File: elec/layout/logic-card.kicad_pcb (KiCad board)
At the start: 2 copper layers, 40 x 40 mm, 0 parts

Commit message: progress
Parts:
- added C1: 1uF, Capacitor_SMD:C_0402_1005Metric, F.Cu at (84.7, 136.4)
- added C10: 1uF, Capacitor_SMD:C_0402_1005Metric, F.Cu at (123.4, 146.3)
- added C11: 100nF, Capacitor_SMD:C_0402_1005Metric, F.Cu at (123.4, 134.4)
- added C12: 100nF, Capacitor_SMD:C_0402_1005Metric, F.Cu at (123.4, 142.4)
- added C13: 100nF, Capacitor_SMD:C_0402_1005Metric, F.Cu at (128.3, 146.3)
- added C14: 1uF, Capacitor_SMD:C_0402_1005Metric, F.Cu at (117.0, 149.6)
- added C2: 1uF, Capacitor_SMD:C_0402_1005Metric, F.Cu at (117.0, 145.6)
- added C3: 20pF, Capacitor_SMD:C_0402_1005Metric, F.Cu at (111.9, 146.7)
- added C4: 20pF, Capacitor_SMD:C_0402_1005Metric, F.Cu at (119.8, 146.7)
- added C5: 100nF, Capacitor_SMD:C_0402_1005Metric, F.Cu at (106.1, 145.0)
- added C6: 100nF, Capacitor_SMD:C_0402_1005Metric, F.Cu at (123.4, 138.4)
- added C7: 100nF, Capacitor_SMD:C_0402_1005Metric, F.Cu at (128.3, 142.4)
- added C8: 100nF, Capacitor_SMD:C_0402_1005Metric, F.Cu at (128.3, 134.4)
- added C9: 100nF, Capacitor_SMD:C_0402_1005Metric, F.Cu at (128.3, 138.4)
- added R1: 18k, Resistor_SMD:R_0402_1005Metric, F.Cu at (102.5, 147.6)
- added R10: 10k, Resistor_SMD:R_0402_1005Metric, F.Cu at (77.9, 137.0)
- added R2: 10k, Resistor_SMD:R_0402_1005Metric, F.Cu at (77.9, 131.9)
- added R3: 1k, Resistor_SMD:R_0402_1005Metric, F.Cu at (70.9, 137.0)
- added R4: 27R, Resistor_SMD:R_0402_1005Metric, F.Cu at (82.2, 118.4)
- added R5: 27R, Resistor_SMD:R_0402_1005Metric, F.Cu at (70.9, 126.7)
- added R6: 10k, Resistor_SMD:R_0402_1005Metric, F.Cu at (77.8, 141.6)
- added R7: 10k, Resistor_SMD:R_0402_1005Metric, F.Cu at (63.9, 141.6)
- added R8: 1k, Resistor_SMD:R_0402_1005Metric, F.Cu at (64.0, 126.7)
- added R9: 10k, Resistor_SMD:R_0402_1005Metric, F.Cu at (70.8, 141.6)
- added U1: <help! no value>, lib:SOT-23-5_L3.0-W1.7-P0.95-LS2.8-BL, F.Cu at (67.1, 111.6)
- added U10: <help! no value>, lib:HDR-TH_8P-P1.27-V-M, F.Cu at (100.8, 137.1)
- added U11: <help! no value>, lib:HDR-TH_8P-P1.27-V-M, F.Cu at (143.8, 137.0)
- added U2: <help! no value>, lib:BAT-TH_BH-AAA-A1AJ024, F.Cu at (233.7, 136.6)
- added U3: <help! no value>, lib:LQFN-56_L7.0-W7.0-P0.4-EP, F.Cu at (115.4, 138.0)
- added U4: <help! no value>, lib:OSC-SMD_4P-L3.2-W2.5-BL, F.Cu at (115.8, 146.6)
- added U5: <help! no value>, lib:WSON-8_L6.0-W8.0-P1.27-BL-EP, F.Cu at (116.0, 124.5)
- added U6: <help! no value>, lib:SW-SMD_4P-L5.1-W5.1-P3.70-LS6.5-TL-2, F.Cu at (116.8, 100.2)
- added U7: <help! no value>, lib:SW-SMD_4P-L5.1-W5.1-P3.70-LS6.5-TL-2, F.Cu at (116.8, 91.9)
- added U8: <help! no value>, lib:KEY-TH_CPG1511F01S0X, F.Cu at (98.1, 79.2)
- added U9: <help! no value>, lib:KEY-TH_CPG1511F01S0X, F.Cu at (90.6, 100.3)

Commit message: update the rp2040 kit
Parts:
- removed the U6 at (116.8, 100.2)
- added J1: <help! no value>, lib:USB-C-SMD_KH-TYPE-C-16P, F.Cu at (173.4, 81.8)
- added R10: 10k, Resistor_SMD:R_0402_1005Metric, F.Cu at (150.6, 71.2)
- added R13: 1.5K, Resistor_SMD:R_0603_1608Metric, F.Cu at (155.2, 108.1)
- added R14: 100, Resistor_SMD:R_0603_1608Metric, F.Cu at (155.0, 102.5)
- added R15: 100, Resistor_SMD:R_0603_1608Metric, F.Cu at (155.2, 97.3)
- added R9: 10k, Resistor_SMD:R_0402_1005Metric, F.Cu at (137.5, 70.3)
- added U12: <help! no value>, Connector_PinHeader_1.27mm:PinHeader_1x04_P1.27mm_Vertical, F.Cu at (165.1, 102.7)
- added U13: <help! no value>, lib:SOT-323-3_L2.0-W1.3-P1.30-LS2.1-BR, F.Cu at (155.1, 105.2)
- added U14: <help! no value>, lib:SOT-323-3_L2.0-W1.3-P1.30-LS2.1-BR, F.Cu at (155.1, 100.2)
- added U15: <help! no value>, lib:SOT-323-3_L2.0-W1.3-P1.30-LS2.1-BR, F.Cu at (155.2, 94.7)
- added U8: <help! no value>, lib:SW-SMD_4P-L5.1-W5.1-P3.70-LS6.5-TL-2, F.Cu at (158.8, 70.9)
- R11: renamed from R9; footprint Resistor_SMD:R_0402_1005Metric -> Resistor_SMD:R_0603_1608Metric
- R12: renamed from R10; footprint Resistor_SMD:R_0402_1005Metric -> Resistor_SMD:R_0603_1608Metric
- U10: renamed from U9; footprint lib:KEY-TH_CPG1511F01S0X -> lib:SW-TH_4P-L12.0-W12.0-P5.00-LS12.5-EH
- U2: moved to B.Cu
- U9: renamed from U8; footprint lib:KEY-TH_CPG1511F01S0X -> lib:SW-TH_4P-L12.0-W12.0-P5.00-LS12.5-EH
- moved U2 112.8 mm to (137.9, 77.1), turned to 90 degrees
- moved R7 110.5 mm to (150.5, 73.0)
- moved R5 105.0 mm to (166.9, 84.1), turned to 180 degrees
- moved R8 104.2 mm to (150.6, 68.8), turned to 180 degrees
- moved R2 93.9 mm to (156.2, 80.0), turned to -90 degrees
- moved R4 92.1 mm to (166.9, 82.0)
- moved R6 90.7 mm to (137.5, 73.3), turned to 180 degrees
- moved U1 90.3 mm to (150.9, 78.2)
- moved R1 88.6 mm to (156.2, 77.1), turned to -90 degrees
- moved C1 85.6 mm to (150.5, 81.7)
- moved R3 77.8 mm to (142.8, 107.3), turned to -90 degrees
- moved R11 75.8 mm to (131.3, 95.9), turned to 90 degrees
- moved C14 62.2 mm to (146.1, 94.6), turned to 90 degrees
- moved C2 59.6 mm to (147.7, 94.6), turned to 90 degrees
- moved R12 59.3 mm to (130.4, 109.4), turned to -90 degrees
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- renumbered U10 to U3, U3 to U4, U4 to U5, U5 to U6
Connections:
- net input renamed xin
- net output renamed p1
- R11 pad 1: vcc-3 -> vcc-4
- R11 pad 2: gpio13 -> gpio0
- R12 pad 1: vcc-4 -> vcc-5
- R6 pad 2: run -> p1-1
- U10 pad 2: gnd-5 -> gpio14
- U4 pad 1: iovdd -> vcc-1
- U4 pad 10: iovdd -> vcc-1
- U4 pad 22: iovdd -> vcc-1
- U4 pad 26: run -> p1-1
- U4 pad 33: iovdd -> vcc-1
- U4 pad 42: iovdd -> vcc-1
- U4 pad 49: iovdd -> vcc-1
- U7 pad 1: cs -> p1-1
- U7 pad 2: cs -> p1-1
- U9 pad 1: gpio13 -> gpio0
- U9 pad 2: gnd-4 -> gpio0
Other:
- board size 40 x 40 mm -> 76 x 68 mm

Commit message: finished up
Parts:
- added R12: 10k, Resistor_SMD:R_0402_1005Metric, F.Cu at (108.1, 97.5)
- added R13: 10k, Resistor_SMD:R_0402_1005Metric, F.Cu at (108.0, 98.8)
- added R14: 10k, Resistor_SMD:R_0402_1005Metric, F.Cu at (108.0, 100.0)
- added R16: 10k, Resistor_SMD:R_0402_1005Metric, F.Cu at (108.0, 102.6)
- added R17: 10k, Resistor_SMD:R_0402_1005Metric, F.Cu at (108.0, 103.8)
- added U4: <help! no value>, lib:SOD-123_L2.8-W1.8-LS3.7-RD, F.Cu at (106.2, 81.6)
- added U8: <help! no value>, lib:SOD-123_L2.8-W1.8-LS3.7-RD, F.Cu at (165.6, 78.5)
- R10: footprint Resistor_SMD:R_0402_1005Metric -> Resistor_SMD:R_0603_1608Metric
- R15: value 100 -> 10k; footprint Resistor_SMD:R_0603_1608Metric -> Resistor_SMD:R_0402_1005Metric
- R18: renamed from R12; value 10k -> 1.5K
- R19: renamed from R13; value 1.5K -> 100
- R8: value 1k -> 10k
- moved R15 47.4 mm to (108.0, 101.3), turned to 0 degrees
- moved R10 32.3 mm to (130.3, 96.3), turned to 90 degrees
- moved R18 24.6 mm to (155.0, 108.1), turned to 180 degrees
- moved R4 17.7 mm to (152.0, 91.6)
- moved R5 17.4 mm to (152.0, 93.0)
- moved R9 13.1 mm to (150.6, 69.8), turned to 0 degrees
- moved R8 13.1 mm to (137.6, 70.4)
- moved C7 9.82 mm to (150.4, 98.3), turned to 0 degrees
- moved R11 8.76 mm to (130.3, 104.6), turned to -90 degrees
- moved R19 5.60 mm to (155.1, 102.5)
- moved R20 5.40 mm to (155.1, 97.1)
- moved C6 3.00 mm to (145.7, 107.0)
- moved C4 2.13 mm to (144.2, 109.6)
- moved U6 2.12 mm to (141.1, 108.9)
- moved C3 2.02 mm to (138.2, 109.0)
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- renumbered R14 to R20, U8 to U10, U9 to U11, U10 to U12, U11 to U13, U12 to U14, U13 to U15, U14 to U16, U15 to U17, U4 to U5, U5 to U6, U6 to U7, U7 to U9
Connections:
- R10 pad 2: cs -> gpio0
- R11 pad 1: vcc-4 -> vcc-1
- R11 pad 2: gpio0 -> gpio14
- R15 pad 1: p1-4 -> vcc-1
- R15 pad 2: b_sink -> gpio4
- R18 pad 1: vcc-5 -> p1-2
- R18 pad 2: gpio14 -> r_sink
- R19 pad 1: p1-2 -> p1-3
- R19 pad 2: r_sink -> g_sink
- R20 pad 1: p1-3 -> p1-4
- R20 pad 2: g_sink -> b_sink
- R3 pad 2: out -> out-1
- R8 pad 1: cs -> vcc-1
- R8 pad 2: gnd -> p1-1
- R9 pad 2: p1-1 -> cs
- U11 pad 3: gnd-1 -> gnd
- U11 pad 4: gnd-1 -> gnd
- U12 pad 3: gnd-2 -> gnd
- U12 pad 4: gnd-2 -> gnd
- U13 pad 8: out-1 -> out-2
- U3 pad 8: vcc -> out
- U6 pad 3: out -> out-1
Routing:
- net vcc-1: track 0.00 -> 240.9 mm, vias 0 -> 9
- net vcc: track 0.00 -> 69.4 mm, vias 0 -> 2
- net p1-1: track 0.00 -> 51.6 mm, vias 0 -> 2
- net cs: track 0.00 -> 50.5 mm, vias 0 -> 2
- net plus: track 0.00 -> 40.5 mm
- net gpio14: track 0.00 -> 37.7 mm
- net gpio0: track 0.00 -> 35.9 mm
- net gpio6: track 0.00 -> 33.4 mm
- net gpio5: track 0.00 -> 33.0 mm
- net gpio1: track 0.00 -> 32.8 mm
- net gpio4: track 0.00 -> 32.6 mm
- net gpio2: track 0.00 -> 32.5 mm
- net gpio3: track 0.00 -> 32.3 mm
- net vcc-2: track 0.00 -> 30.4 mm, vias 0 -> 2
- net dm: track 0.00 -> 26.3 mm, vias 0 -> 2
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- added copper zone on B.Cu, net gnd
- added copper zone on F.Cu, net gnd
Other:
- outline, holes or cut-outs redrawn

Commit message: stabil junge
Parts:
- removed the R8 at (137.6, 70.4)
- removed the R9 at (150.6, 69.8)
- removed the U10 at (158.8, 70.9)
- added U8: <help! no value>, lib:SW-SMD_4P-L5.1-W5.1-P3.70-LS6.5-TL-2, F.Cu at (131.4, 71.4)
- U13, U3: footprint lib:HDR-TH_8P-P1.27-V-M -> lib:HDR-TH_8P-P2.00-V-M
- moved U9 27.4 mm to (158.8, 71.0)
- moved R11 0.40 mm to (107.6, 98.8)
- moved R12 0.40 mm to (107.6, 100.0)
- moved R13 0.40 mm to (107.6, 101.3)
- moved R14 0.40 mm to (107.6, 102.6)
- moved R15 0.40 mm to (107.6, 103.8)
- moved R10 0.40 mm to (107.7, 97.5)
- renumbered R12 to R10, R13 to R11, R14 to R12, R15 to R13, R16 to R14, R17 to R15, R18 to R16, R19 to R17, R20 to R18, R10 to R8, R11 to R9, U8 to U10
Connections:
- R16 pad 1: p1-2 -> p1-1
- R17 pad 1: p1-3 -> p1-2
- R18 pad 1: p1-4 -> p1-3
- R6 pad 2: p1-1 -> run
- U14 pad 1: p1-2 -> p1-1
- U14 pad 2: p1-3 -> p1-2
- U14 pad 4: p1-4 -> p1-3
- U5 pad 26: p1-1 -> run
- U9 pad 1: p1-1 -> cs
- U9 pad 2: p1-1 -> cs
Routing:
- net run: track 0.00 -> 48.7 mm, vias 0 -> 2
- net p1-1: track 51.6 -> 11.5 mm, vias 2 -> 0
- net p1-4: track 9.92 -> 0.00 mm
- net vcc-1: track 240.9 -> 234.8 mm
- net gpio6: track 33.4 -> 37.3 mm
- net cs: track 50.5 -> 47.3 mm
- net gpio1: track 32.8 -> 35.9 mm
- net plus: track 40.5 -> 37.9 mm
- net gpio5: track 33.0 -> 34.9 mm
- net p1-2: track 11.5 -> 9.62 mm
- net gpio2: track 32.5 -> 34.0 mm
- net out: track 25.2 -> 26.7 mm
- net gpio4: track 32.6 -> 33.3 mm
- net gpio3: track 32.3 -> 32.8 mm

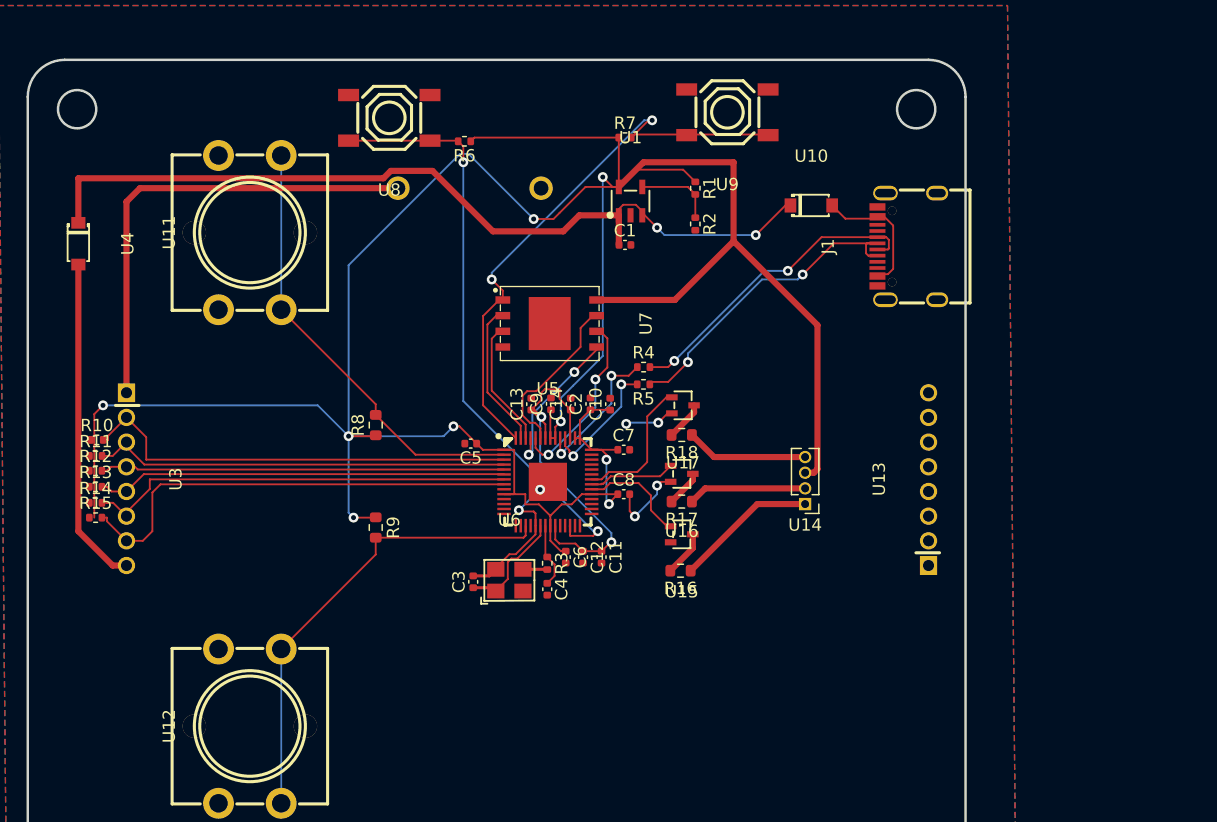
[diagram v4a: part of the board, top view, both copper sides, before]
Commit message: update gitignore
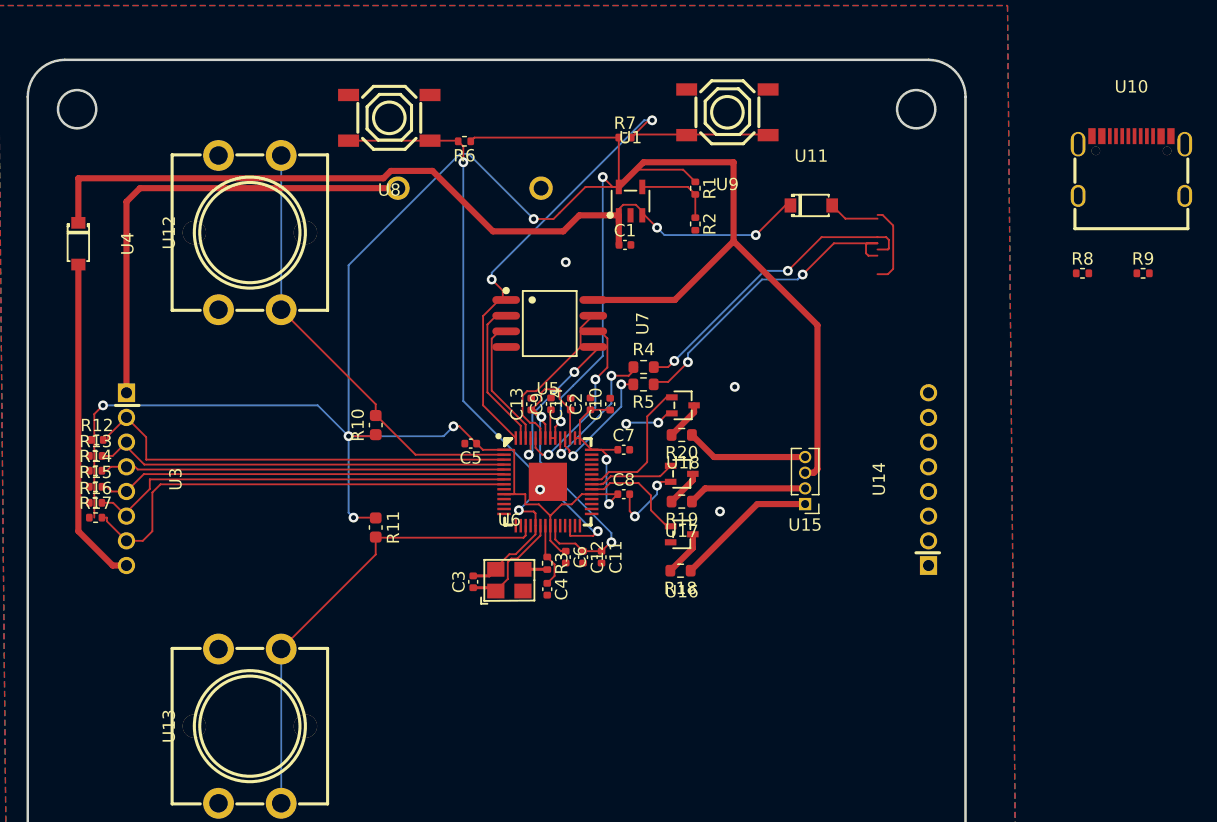
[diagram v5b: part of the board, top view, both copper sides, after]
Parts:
- removed J1: <help! no value>, lib:USB-C-SMD_KH-TYPE-C-16P
- added R8: 5.1k, lib:R0402, F.Cu at (187.6, 84.0)
- added R9: 5.1k, lib:R0402, F.Cu at (192.5, 84.0)
- added U10: <help! no value>, lib:USB-C-SMD_KH-TYPE-C-16P, F.Cu at (191.5, 75.3)
- C1, C10, C11, C12, C13, C14, C2, C3, C4, C5, C6, C7, C8, C9: footprint Capacitor_SMD:C_0402_1005Metric -> lib:C0402
- R1, R2, R3, R6, R7: footprint Resistor_SMD:R_0402_1005Metric -> lib:R0402
- R10: renamed from R8; footprint Resistor_SMD:R_0603_1608Metric -> lib:C0603
- R11: renamed from R9; footprint Resistor_SMD:R_0603_1608Metric -> lib:C0603
- R12: renamed from R10; footprint Resistor_SMD:R_0402_1005Metric -> lib:R0402
- R13: renamed from R11; footprint Resistor_SMD:R_0402_1005Metric -> lib:R0402
- R14: renamed from R12; footprint Resistor_SMD:R_0402_1005Metric -> lib:R0402
- R15: renamed from R13; footprint Resistor_SMD:R_0402_1005Metric -> lib:R0402
- R16: renamed from R14; footprint Resistor_SMD:R_0402_1005Metric -> lib:R0402
- R17: renamed from R15; footprint Resistor_SMD:R_0402_1005Metric -> lib:R0402
- R18: renamed from R16; footprint Resistor_SMD:R_0603_1608Metric -> lib:R0603
- R19: renamed from R17; footprint Resistor_SMD:R_0603_1608Metric -> lib:R0603
- R20: renamed from R18; footprint Resistor_SMD:R_0603_1608Metric -> lib:R0603
- R4, R5: footprint Resistor_SMD:R_0402_1005Metric -> lib:R0603
- U7: footprint lib:WSON-8_L6.0-W8.0-P1.27-BL-EP -> lib:SOIC-8_L5.3-W5.3-P1.27-LS8.0-BL
- renumbered U10 to U11, U11 to U12, U12 to U13, U13 to U14, U14 to U15, U15 to U16, U16 to U17, U17 to U18
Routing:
- net gnd: vias 6 -> 9

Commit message: update the layout
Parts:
- removed the R17 at (107.6, 103.8)
- R17: renamed from R18; value 1.5K -> 1.5k
- R4, R5: footprint lib:R0603 -> lib:R0402
- moved R9 24.7 mm to (168.1, 79.8), turned to 180 degrees
- moved R8 19.5 mm to (168.1, 83.5), turned to 180 degrees
- moved U10 19.2 mm to (173.4, 81.8), turned to 90 degrees
- moved U11 1.30 mm to (165.5, 77.2)
- renumbered R19 to R18, R20 to R19
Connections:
- U3 pad 7: gpio6 -> gnd
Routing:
- net gpio6: track 37.3 -> 0.00 mm
- net gnd: track 22.6 -> 25.4 mm, vias 9 -> 19
- net CC1: track 0.00 -> 2.59 mm
- net CC2: track 0.00 -> 2.51 mm
- net vcc-1: track 234.8 -> 236.8 mm
- net vcc: track 69.4 -> 70.4 mm
- net sck: track 14.6 -> 15.4 mm
- net vcc-3: track 10.7 -> 11.3 mm
